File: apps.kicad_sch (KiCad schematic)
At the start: 58 parts, among them J1 1-776280-1, J2 SWD, J3 UART, J4 Conn_01x04, Q1 AO3400A, SW1 SW_Push, SW2 SW_Push, U1 STM32F103C8Tx, U2 MCP2551, U3 AMS1117-5.0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

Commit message: Changed SS49E footprint and updated to KiCAD 9
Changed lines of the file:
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@@
 (kicad_sch
-	(version 20231120)
+	(version 20250114)
 	(generator "eeschema")
-	(generator_version "8.0")
+	(generator_version "9.0")
 	(paper "A4")
 	(title_block
@@
 		(comment 2 "Owen Smith")
 	)
+	(rectangle
+		(start 24.13 40.64)
+		(end 59.69 91.44)
+		(stroke
+			(width 0)
+			(type default)
+		)
+		(fill
+			(type none)
+		)
+	)
+	(rectangle
+		(start 50.8 139.7)
+		(end 130.81 184.15)
+		(stroke
+			(width 0)
+			(type default)
+		)
+		(fill
+			(type none)
+		)
+	)
+	(rectangle
+		(start 156.21 25.4)
+		(end 262.89 140.97)
+		(stroke
+			(width 0)
+			(type default)
+		)
+		(fill
+			(type none)
+		)
+	)
+	(rectangle
+		(start 50.8 100.33)
+		(end 124.46 125.73)
+		(stroke
+			(width 0)
+			(type default)
+		)
+		(fill
+			(type none)
+		)
+	)
+	(rectangle
+		(start 68.58 58.42)
+		(end 106.68 91.44)
+		(stroke
+			(width 0)
+			(type default)
+		)
+		(fill
+			(type none)
+		)
+	)
+	(rectangle
+		(start 68.58 26.035)
+		(end 135.89 50.165)
+		(stroke
+			(width 0)
+			(type default)
+		)
+		(fill
+			(type none)
+		)
+	)
+	(text "MCU"
+		(exclude_from_sim no)
+		(at 160.02 22.86 0)
+		(effects
+			(font
+				(size 2 2)
+			)
+		)
+	)
+	(text "Reset and calibration buttons"
+		(exclude_from_sim no)
+		(at 73.66 99.06 0)
+		(effects
+			(font
+				(size 2 2)
+			)
+		)
+	)
+	(text "3V3 LDO"
+		(exclude_from_sim no)
+		(at 74.93 55.88 0)
+		(effects
+			(font
+				(size 2 2)
+			)
+		)
+	)
+	(text "1u for each VDD\n+ extra 100n for VDDA"
+		(exclude_from_sim no)
+		(at 242.57 123.19 0)
+		(effects
+			(font
+				(size 1 1)
+			)
+		)
+	)
+	(text "J4 allows disconnection during real use"
+		(exclude_from_sim no)
+		(at 90.17 123.19 0)
+		(effects
+			(font
+				(size 1 1)
+			)
+		)
+	)
+	(text "Main connector"
+		(exclude_from_sim no)
+		(at 35.56 38.1 0)
+		(effects
+			(font
+				(size 2 2)
+			)
+		)
+	)
+	(text "CAN Transceiver"
+		(exclude_from_sim no)
+		(at 63.5 138.43 0)
+		(effects
+			(font
+				(size 2 2)
+			)
+		)
+	)
+	(text "5V LDO"
+		(exclude_from_sim no)
+		(at 73.66 24.13 0)
+		(effects
+			(font
+				(size 2 2)
+			)
+		)
+	)
 	(junction
 		(at 240.03 128.27)
@@
 		)
 	)
-	(rectangle
-		(start 24.13 40.64)
-		(end 59.69 91.44)
-		(stroke
-			(width 0)
-			(type default)
-		)
-		(fill
-			(type none)
-		)
-	)
-	(rectangle
-		(start 50.8 139.7)
-		(end 130.81 184.15)
-		(stroke
-			(width 0)
-			(type default)
-		)
-		(fill
-			(type none)
-		)
-	)
-	(rectangle
-		(start 156.21 25.4)
-		(end 262.89 140.97)
-		(stroke
-			(width 0)
-			(type default)
-		)
-		(fill
-			(type none)
-		)
-	)
-	(rectangle
-		(start 50.8 100.33)
-		(end 124.46 125.73)
-		(stroke
-			(width 0)
-			(type default)
-		)
-		(fill
-			(type none)
-		)
-	)
-	(rectangle
-		(start 68.58 58.42)
-		(end 106.68 91.44)
-		(stroke
-			(width 0)
-			(type default)
-		)
-		(fill
-			(type none)
-		)
-	)
-	(rectangle
-		(start 68.58 26.035)
-		(end 135.89 50.165)
-		(stroke
-			(width 0)
-			(type default)
-		)
-		(fill
-			(type none)
-		)
-	)
-	(text "MCU"
-		(exclude_from_sim no)
-		(at 160.02 22.86 0)
-		(effects
-			(font
-				(size 2 2)
-			)
-		)
-	)
-	(text "Reset and calibration buttons"
-		(exclude_from_sim no)
-		(at 73.66 99.06 0)
-		(effects
-			(font
-				(size 2 2)
-			)
-		)
-	)
-	(text "3V3 LDO"
-		(exclude_from_sim no)
-		(at 74.93 55.88 0)
-		(effects
-			(font
-				(size 2 2)
-			)
-		)
-	)
-	(text "1u for each VDD\n+ extra 100n for VDDA"
-		(exclude_from_sim no)
-		(at 242.57 123.19 0)
-		(effects
-			(font
-				(size 1 1)
-			)
-		)
-	)
-	(text "J4 allows disconnection during real use"
-		(exclude_from_sim no)
-		(at 90.17 123.19 0)
-		(effects
-			(font
-				(size 1 1)
-			)
-		)
-	)
-	(text "Main connector"
-		(exclude_from_sim no)
-		(at 35.56 38.1 0)
-		(effects
-			(font
-				(size 2 2)
-			)
-		)
-	)
-	(text "CAN Transceiver"
-		(exclude_from_sim no)
-		(at 63.5 138.43 0)
-		(effects
-			(font
-				(size 2 2)
-			)
-		)
-	)
-	(text "5V LDO"
-		(exclude_from_sim no)
-		(at 73.66 24.13 0)
-		(effects
-			(font
-				(size 2 2)
-			)
-		)
-	)
 	(label "HSE_IN"
 		(at 176.53 54.61 0)
-		(fields_autoplaced yes)
 		(effects
 			(font
@@
 	(label "HSE_OUT"
 		(at 176.53 52.07 0)
-		(fields_autoplaced yes)
 		(effects
 			(font
@@
 	(label "UART_RX"
 		(at 226.06 67.31 0)
-		(fields_autoplaced yes)
 		(effects
 			(font
@@
 	(label "UART_TX"
 		(at 226.06 64.77 0)
-		(fields_autoplaced yes)
 		(effects
 			(font
@@
 		(at 241.3 50.8)
 		(size 19.05 5.08)
+		(exclude_from_sim no)
+		(in_bom yes)
+		(on_board yes)
+		(dnp no)
 		(fields_autoplaced yes)
 		(stroke
@@
 		(at 241.3 39.37)
 		(size 19.05 5.08)
+		(exclude_from_sim no)
+		(in_bom yes)
+		(on_board yes)
+		(dnp no)
 		(fields_autoplaced yes)
 		(stroke
@@
 		)
 	)
+	(embedded_fonts no)
 )

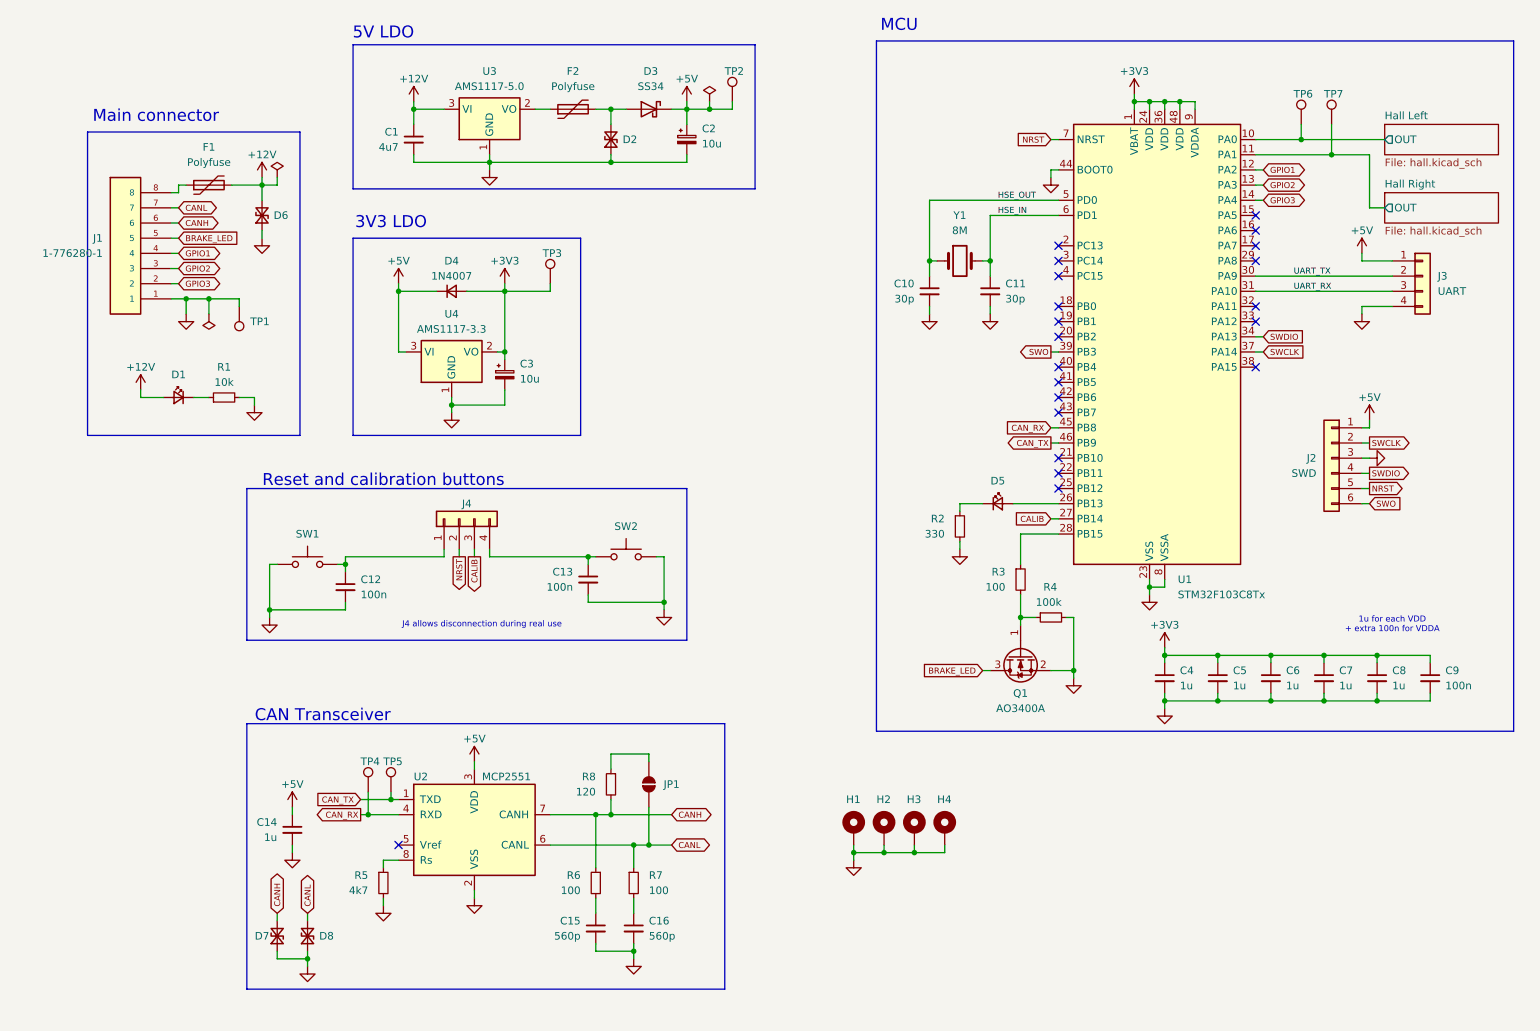
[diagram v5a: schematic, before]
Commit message: Updated CAN Transceiver and LDO
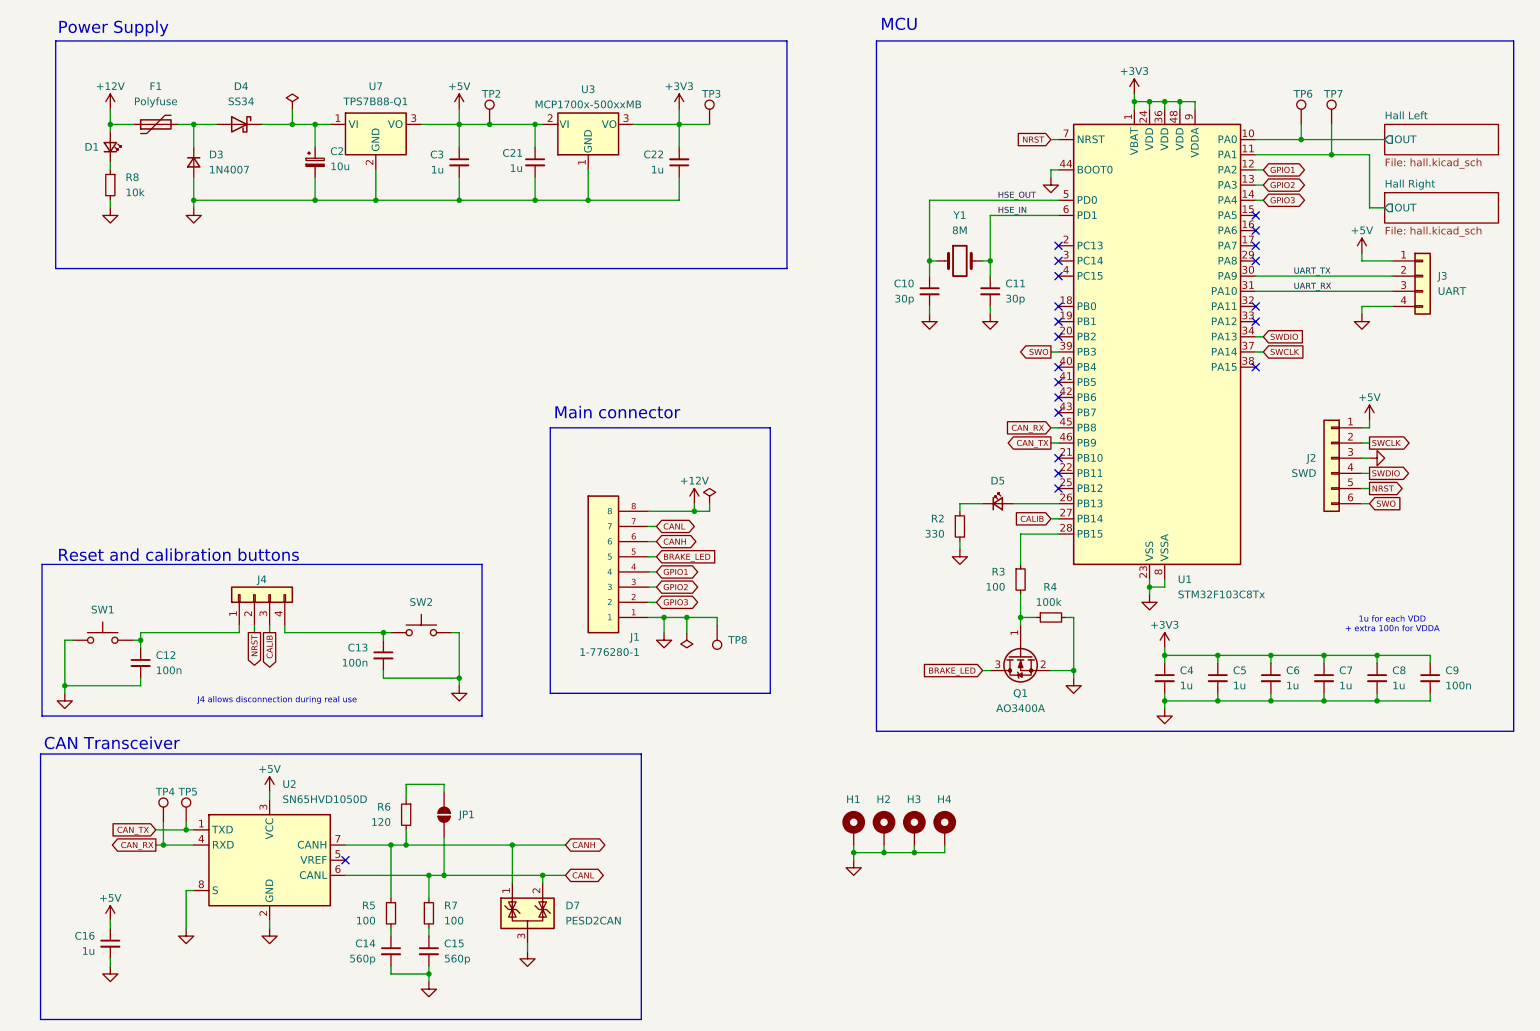
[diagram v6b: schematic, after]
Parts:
- removed C1: 4u7, Capacitor_SMD:C_0805_2012Metric, symbol Device:C_Small
- removed C3: 10u, Capacitor_SMD:CP_Elec_6.3x5.4, symbol Device:C_Polarized_Small
- removed D2: H5VL10B, symbol Device:D_TVS_Small
- removed D3: SS34, Diode_SMD:D_SMA, symbol Diode:SS34
- removed D4: 1N4007, Diode_SMD:D_SOD-123F, symbol Device:D_Small
- removed D6, D7, D8: UDD32C12L01-ES, Diode_SMD:D_SOD-323, symbol Device:D_TVS_Small
- removed F2: Polyfuse, Resistor_SMD:R_0805_2012Metric, symbol Device:Polyfuse
- removed R1: 10k, Resistor_SMD:R_0603_1608Metric, symbol Device:R_Small
- removed TP1: TestPoint, TestPoint:TestPoint_Keystone_5000-5004_Miniature, symbol Connector:TestPoint
- removed U2: MCP2551, Package_SO:SOIC-8_3.9x4.9mm_P1.27mm, symbol Interface_CAN_LIN:MCP2551-I-SN
- removed U3: AMS1117-5.0, Package_TO_SOT_SMD:SOT-223-3_TabPin2, symbol Regulator_Linear:AMS1117-5.0
- removed U4: AMS1117-3.3, Package_TO_SOT_SMD:SOT-223-3_TabPin2, symbol Regulator_Linear:AMS1117-3.3
- added C21, C22, C3: 1u, Capacitor_SMD:C_0603_1608Metric, symbol Device:C_Small
- added D3: 1N4007, Diode_SMD:D_SOD-123F, symbol Device:D_Small
- added D4: SS34, Diode_SMD:D_SMA, symbol Diode:SS34
- added D7: PESD2CAN, Package_TO_SOT_SMD:SOT-23, symbol Power_Protection:NUP2105L
- added TP8: TestPoint, TestPoint:TestPoint_Keystone_5000-5004_Miniature, symbol Connector:TestPoint
- added U2: SN65HVD1050D, Package_SO:SOIC-8_3.9x4.9mm_P1.27mm, symbol Interface_CAN_LIN:SN65HVD1050D
- added U3: MCP1700x-500xxMB, Package_TO_SOT_SMD:SOT-89-3, symbol Regulator_Linear:MCP1700x-500xxMB
- added U7: TPS7B88-Q1, Package_TO_SOT_SMD:TO-252-2, symbol !LJC:L78M
- C14: value 1u -> 560p
- C16: value 560p -> 1u
- R5: value 4k7 -> 100
- R6: value 100 -> 120
- R8: value 120 -> 10k
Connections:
- net +12V: now also F1.1, J1.8; no longer F1.2
- net +3V3: now also C22.2, U3.3 (VO)
- net +5V: now also C16.1, C21.1, C3.1, U2.3 (VCC), U3.2 (VI), U7.3 (VO); no longer C14.1, C2.1
- net CANH: now also R5.1, R6.2, D7.1 (K), U2.7 (CANH); no longer R6.1, R8.2
- net CANL: now also D7.2 (K), U2.6 (CANL)
- net CAN_RX: now also U2.4 (RXD)
- net CAN_TX: now also U2.1 (TXD)
- net GND: now also R8.2, C21.2, C22.1, C3.2, D3.2 (A), D7.3 (A), TP8.1, U2.2 (GND), U2.8 (S), U3.1 (GND), U7.2 (GND); no longer R5.2
- net at C15.1: now also R7.2; no longer R6.2
- net at R8.1: now also D1.1 (K); no longer JP1.1 (A)
- new net: C2.1, D4.1 (K), U7.1 (VI)
- new net: C14.1, R5.2
- new net: D3.1 (K), D4.2 (A), F1.2
- new net: JP1.1 (A), R6.1
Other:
- note added: "Power Supply"
- note removed: "3V3 LDO"
- note removed: "5V LDO"
- moved on the sheet: C12, C13, J1, J4, SW1, SW2
